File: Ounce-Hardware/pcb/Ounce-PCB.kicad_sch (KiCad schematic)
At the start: 5 parts, among them U1 RaspberryPi_Pico_W, U2 RaspberryPi_Pico, U3 RaspberryPi_Pico, U4 RaspberryPi_Pico, U5 RaspberryPi_Pico

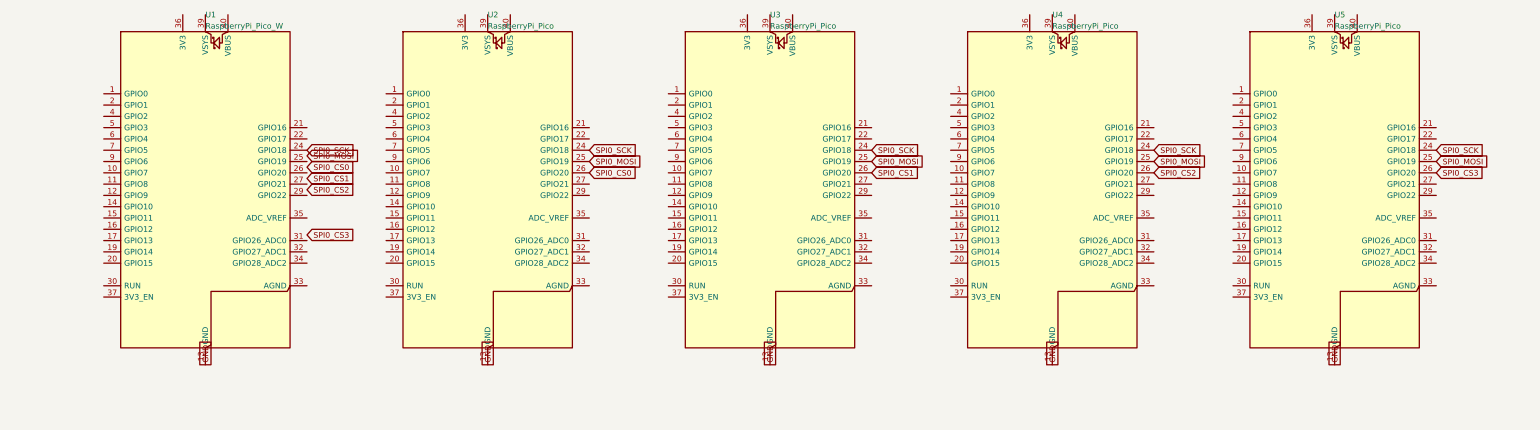
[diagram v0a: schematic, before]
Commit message: Wire the schematic to the four-MISO GPIO standard
The schematic still described the old single-MISO design, and not correctly:

  - servants took MOSI on GPIO19 (pin 25), which under the current standard is
    the servant's MISO *output*. Driving that from the master's MOSI would have
    put two outputs on one wire.
  - servants took CS on GPIO20 (pin 26) rather than GPIO17 (pin 22).
  - the master's MOSI and all four CS labels sat half a pitch (1.27mm) off grid,
    touching no pin at all.
  - no MISO net existed anywhere.

Now carries the eleven nets the firmware actually uses: SCK and MOSI shared,
CS0-3 point to point from GP21/22/26/27 to each servant's GP17, and MISO0-3
back from each servant's GP19 to GP0/4/16/20 on the master.

Two things had to be fixed before any of that could connect:

Labels do not attach to pins by sharing coordinates - ERC reported every label
dangling, including the GND ones that predate this change. Each net now has a
5.08mm wire stub from the pin with the label on its free end.

U1 contributed no pins at all. RaspberryPi_Pico_W was stored as a derived
symbol (extends), which KiCad does not resolve inside a schematic's own symbol
cache, so the master had no connectable pins and reported lib_symbol_mismatch.
Flattened to a standalone symbol carrying its own 40 pins, keeping the Pico W
name and datasheet.

Verified by exporting the netlist with kicad-cli and checking every node
against spi_master.cpp - all eleven nets match pin for pin. ERC now reports no
dangling labels, no isolated labels and no unconnected wire endpoints, down
from 27 such errors.

SVG re-exported to match. The board file is still an outline only: pulling
these nets in needs Update PCB from Schematic in pcbnew, which the CLI cannot
do.

Co-Authored-By: Claude Opus 5 <noreply@anthropic.com>
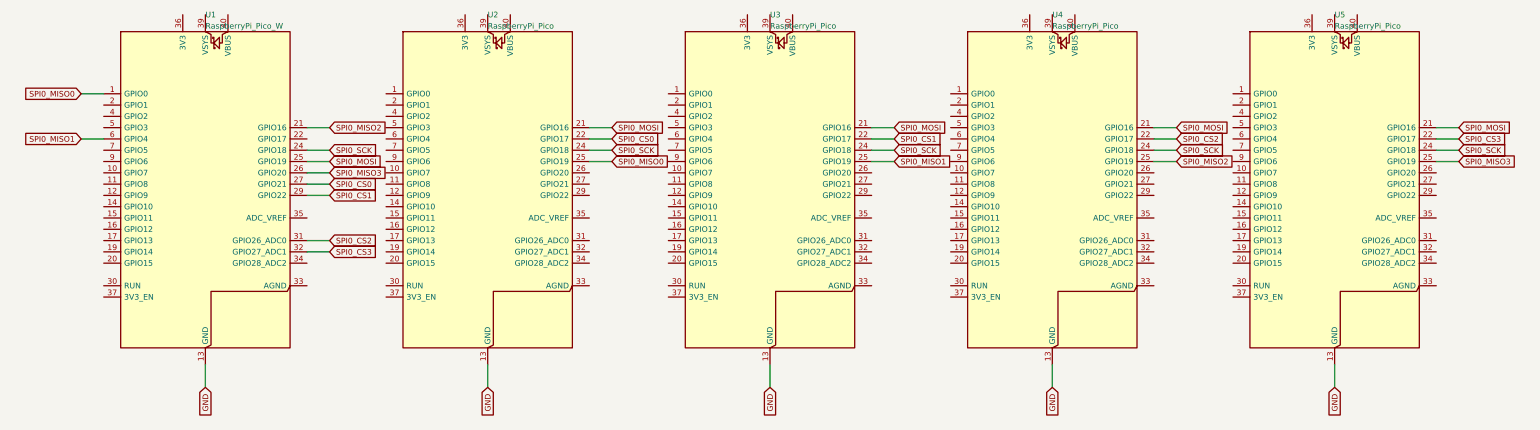
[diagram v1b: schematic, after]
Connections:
- net GND: now also U1.13 (GND), U1.18 (GND), U1.23 (GND), U1.28 (GND), U1.3 (GND), U1.38 (GND), U1.8 (GND)
- net SPI0_CS0: now also U1.27 (GPIO21), U2.22 (GPIO17); no longer U2.26 (GPIO20)
- net SPI0_CS1: now also U1.29 (GPIO22), U3.22 (GPIO17); no longer U3.26 (GPIO20)
- net SPI0_CS2: now also U1.31 (GPIO26_ADC0), U4.22 (GPIO17); no longer U4.26 (GPIO20)
- net SPI0_CS3: now also U1.32 (GPIO27_ADC1), U5.22 (GPIO17); no longer U5.26 (GPIO20)
- net SPI0_MOSI: now also U1.25 (GPIO19), U2.21 (GPIO16), U3.21 (GPIO16), U4.21 (GPIO16), U5.21 (GPIO16); no longer U2.25 (GPIO19), U3.25 (GPIO19), U4.25 (GPIO19), U5.25 (GPIO19)
- net SPI0_SCK: now also U1.24 (GPIO18)
- new net SPI0_MISO0: U1.1 (GPIO0), U2.25 (GPIO19)
- new net SPI0_MISO1: U1.6 (GPIO4), U3.25 (GPIO19)
- new net SPI0_MISO2: U1.21 (GPIO16), U4.25 (GPIO19)
- new net SPI0_MISO3: U1.26 (GPIO20), U5.25 (GPIO19)
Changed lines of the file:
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@@
     )
-  )
-  (global_label "SPI0_SCK" (shape input) (at 73.66 53.34 0)
-    (effects (font (size 1.27 1.27)) (justify left))
-  )
-  (global_label "SPI0_MOSI" (shape input) (at 73.66 54.61 0)
-    (effects (font (size 1.27 1.27)) (justify left))
-  )
-  (global_label "SPI0_CS0" (shape input) (at 73.66 57.15 0)
-    (effects (font (size 1.27 1.27)) (justify left))
-  )
-  (global_label "SPI0_CS1" (shape input) (at 73.66 59.69 0)
-    (effects (font (size 1.27 1.27)) (justify left))
-  )
-  (global_label "SPI0_CS2" (shape input) (at 73.66 62.23 0)
-    (effects (font (size 1.27 1.27)) (justify left))
-  )
-  (global_label "SPI0_CS3" (shape input) (at 73.66 72.39 0)
-    (effects (font (size 1.27 1.27)) (justify left))
-  )
-  (global_label "GND" (shape passive) (at 50.80 101.60 270)
-    (effects (font (size 1.27 1.27)) (justify left))
-  )
-  (global_label "SPI0_SCK" (shape input) (at 137.16 53.34 0)
-    (effects (font (size 1.27 1.27)) (justify left))
-  )
-  (global_label "SPI0_MOSI" (shape input) (at 137.16 55.88 0)
-    (effects (font (size 1.27 1.27)) (justify left))
-  )
-  (global_label "SPI0_CS0" (shape input) (at 137.16 58.42 0)
-    (effects (font (size 1.27 1.27)) (justify left))
-  )
-  (global_label "GND" (shape passive) (at 114.30 101.60 270)
-    (effects (font (size 1.27 1.27)) (justify left))
-  )
-  (global_label "SPI0_SCK" (shape input) (at 200.66 53.34 0)
-    (effects (font (size 1.27 1.27)) (justify left))
-  )
-  (global_label "SPI0_MOSI" (shape input) (at 200.66 55.88 0)
-    (effects (font (size 1.27 1.27)) (justify left))
-  )
-  (global_label "SPI0_CS1" (shape input) (at 200.66 58.42 0)
-    (effects (font (size 1.27 1.27)) (justify left))
-  )
-  (global_label "GND" (shape passive) (at 177.80 101.60 270)
-    (effects (font (size 1.27 1.27)) (justify left))
-  )
-  (global_label "SPI0_SCK" (shape input) (at 264.16 53.34 0)
-    (effects (font (size 1.27 1.27)) (justify left))
-  )
-  (global_label "SPI0_MOSI" (shape input) (at 264.16 55.88 0)
-    (effects (font (size 1.27 1.27)) (justify left))
-  )
-  (global_label "SPI0_CS2" (shape input) (at 264.16 58.42 0)
-    (effects (font (size 1.27 1.27)) (justify left))
-  )
-  (global_label "GND" (shape passive) (at 241.30 101.60 270)
-    (effects (font (size 1.27 1.27)) (justify left))
-  )
-  (global_label "SPI0_SCK" (shape input) (at 327.66 53.34 0)
-    (effects (font (size 1.27 1.27)) (justify left))
-  )
-  (global_label "SPI0_MOSI" (shape input) (at 327.66 55.88 0)
-    (effects (font (size 1.27 1.27)) (justify left))
-  )
-  (global_label "SPI0_CS3" (shape input) (at 327.66 58.42 0)
-    (effects (font (size 1.27 1.27)) (justify left))
-  )
-  (global_label "GND" (shape passive) (at 304.80 101.60 270)
-    (effects (font (size 1.27 1.27)) (justify left))
   )
   (sheet_instances (path "/" (page "1")))
@@
     )
   )
+  (wire (pts (xy 73.66 53.34) (xy 78.74 53.34))
+    (stroke (width 0) (type default))
+  )
+  (wire (pts (xy 73.66 55.88) (xy 78.74 55.88))
+    (stroke (width 0) (type default))
+  )
+  (wire (pts (xy 73.66 60.96) (xy 78.74 60.96))
+    (stroke (width 0) (type default))
+  )
+  (wire (pts (xy 73.66 63.50) (xy 78.74 63.50))
+    (stroke (width 0) (type default))
+  )
+  (wire (pts (xy 73.66 73.66) (xy 78.74 73.66))
+    (stroke (width 0) (type default))
+  )
+  (wire (pts (xy 73.66 76.20) (xy 78.74 76.20))
+    (stroke (width 0) (type default))
+  )
+  (wire (pts (xy 27.94 40.64) (xy 22.86 40.64))
+    (stroke (width 0) (type default))
+  )
+  (wire (pts (xy 27.94 50.80) (xy 22.86 50.80))
+    (stroke (width 0) (type default))
+  )
+  (wire (pts (xy 73.66 48.26) (xy 78.74 48.26))
+    (stroke (width 0) (type default))
+  )
+  (wire (pts (xy 73.66 58.42) (xy 78.74 58.42))
+    (stroke (width 0) (type default))
+  )
+  (wire (pts (xy 50.80 101.60) (xy 50.80 106.68))
+    (stroke (width 0) (type default))
+  )
+  (wire (pts (xy 137.16 53.34) (xy 142.24 53.34))
+    (stroke (width 0) (type default))
+  )
+  (wire (pts (xy 137.16 48.26) (xy 142.24 48.26))
+    (stroke (width 0) (type default))
+  )
+  (wire (pts (xy 137.16 50.80) (xy 142.24 50.80))
+    (stroke (width 0) (type default))
+  )
+  (wire (pts (xy 137.16 55.88) (xy 142.24 55.88))
+    (stroke (width 0) (type default))
+  )
+  (wire (pts (xy 114.30 101.60) (xy 114.30 106.68))
+    (stroke (width 0) (type default))
+  )
+  (wire (pts (xy 200.66 53.34) (xy 205.74 53.34))
+    (stroke (width 0) (type default))
+  )
+  (wire (pts (xy 200.66 48.26) (xy 205.74 48.26))
+    (stroke (width 0) (type default))
+  )
+  (wire (pts (xy 200.66 50.80) (xy 205.74 50.80))
+    (stroke (width 0) (type default))
+  )
+  (wire (pts (xy 200.66 55.88) (xy 205.74 55.88))
+    (stroke (width 0) (type default))
+  )
+  (wire (pts (xy 177.80 101.60) (xy 177.80 106.68))
+    (stroke (width 0) (type default))
+  )
+  (wire (pts (xy 264.16 53.34) (xy 269.24 53.34))
+    (stroke (width 0) (type default))
+  )
+  (wire (pts (xy 264.16 48.26) (xy 269.24 48.26))
+    (stroke (width 0) (type default))
+  )
+  (wire (pts (xy 264.16 50.80) (xy 269.24 50.80))
+    (stroke (width 0) (type default))
+  )
+  (wire (pts (xy 264.16 55.88) (xy 269.24 55.88))
+    (stroke (width 0) (type default))
+  )
+  (wire (pts (xy 241.30 101.60) (xy 241.30 106.68))
+    (stroke (width 0) (type default))
+  )
+  (wire (pts (xy 327.66 53.34) (xy 332.74 53.34))
+    (stroke (width 0) (type default))
+  )
+  (wire (pts (xy 327.66 48.26) (xy 332.74 48.26))
+    (stroke (width 0) (type default))
+  )
+  (wire (pts (xy 327.66 50.80) (xy 332.74 50.80))
+    (stroke (width 0) (type default))
+  )
+  (wire (pts (xy 327.66 55.88) (xy 332.74 55.88))
+    (stroke (width 0) (type default))
+  )
+  (wire (pts (xy 304.80 101.60) (xy 304.80 106.68))
+    (stroke (width 0) (type default))
+  )
+  (global_label "SPI0_SCK" (shape input) (at 78.74 53.34 0)
+    (effects (font (size 1.27 1.27)) (justify left))
+  )
+  (global_label "SPI0_MOSI" (shape input) (at 78.74 55.88 0)
+    (effects (font (size 1.27 1.27)) (justify left))
+  )
+  (global_label "SPI0_CS0" (shape input) (at 78.74 60.96 0)
+    (effects (font (size 1.27 1.27)) (justify left))
+  )
+  (global_label "SPI0_CS1" (shape input) (at 78.74 63.50 0)
+    (effects (font (size 1.27 1.27)) (justify left))
+  )
+  (global_label "SPI0_CS2" (shape input) (at 78.74 73.66 0)
+    (effects (font (size 1.27 1.27)) (justify left))
+  )
+  (global_label "SPI0_CS3" (shape input) (at 78.74 76.20 0)
+    (effects (font (size 1.27 1.27)) (justify left))
+  )
+  (global_label "SPI0_MISO0" (shape input) (at 22.86 40.64 180)
+    (effects (font (size 1.27 1.27)) (justify right))
+  )
+  (global_label "SPI0_MISO1" (shape input) (at 22.86 50.80 180)
+    (effects (font (size 1.27 1.27)) (justify right))
+  )
+  (global_label "SPI0_MISO2" (shape input) (at 78.74 48.26 0)
+    (effects (font (size 1.27 1.27)) (justify left))
+  )
+  (global_label "SPI0_MISO3" (shape input) (at 78.74 58.42 0)
+    (effects (font (size 1.27 1.27)) (justify left))
+  )
+  (global_label "GND" (shape input) (at 50.80 106.68 270)
+    (effects (font (size 1.27 1.27)) (justify right))
+  )
+  (global_label "SPI0_SCK" (shape input) (at 142.24 53.34 0)
+    (effects (font (size 1.27 1.27)) (justify left))
+  )
+  (global_label "SPI0_MOSI" (shape input) (at 142.24 48.26 0)
+    (effects (font (size 1.27 1.27)) (justify left))
+  )
+  (global_label "SPI0_CS0" (shape input) (at 142.24 50.80 0)
+    (effects (font (size 1.27 1.27)) (justify left))
+  )
+  (global_label "SPI0_MISO0" (shape input) (at 142.24 55.88 0)
+    (effects (font (size 1.27 1.27)) (justify left))
+  )
+  (global_label "GND" (shape input) (at 114.30 106.68 270)
+    (effects (font (size 1.27 1.27)) (justify right))
+  )
+  (global_label "SPI0_SCK" (shape input) (at 205.74 53.34 0)
+    (effects (font (size 1.27 1.27)) (justify left))
+  )
+  (global_label "SPI0_MOSI" (shape input) (at 205.74 48.26 0)
+    (effects (font (size 1.27 1.27)) (justify left))
+  )
+  (global_label "SPI0_CS1" (shape input) (at 205.74 50.80 0)
+    (effects (font (size 1.27 1.27)) (justify left))
+  )
+  (global_label "SPI0_MISO1" (shape input) (at 205.74 55.88 0)
+    (effects (font (size 1.27 1.27)) (justify left))
+  )
+  (global_label "GND" (shape input) (at 177.80 106.68 270)
+    (effects (font (size 1.27 1.27)) (justify right))
+  )
+  (global_label "SPI0_SCK" (shape input) (at 269.24 53.34 0)
+    (effects (font (size 1.27 1.27)) (justify left))
+  )
+  (global_label "SPI0_MOSI" (shape input) (at 269.24 48.26 0)
+    (effects (font (size 1.27 1.27)) (justify left))
+  )
+  (global_label "SPI0_CS2" (shape input) (at 269.24 50.80 0)
+    (effects (font (size 1.27 1.27)) (justify left))
+  )
+  (global_label "SPI0_MISO2" (shape input) (at 269.24 55.88 0)
+    (effects (font (size 1.27 1.27)) (justify left))
+  )
+  (global_label "GND" (shape input) (at 241.30 106.68 270)
+    (effects (font (size 1.27 1.27)) (justify right))
+  )
+  (global_label "SPI0_SCK" (shape input) (at 332.74 53.34 0)
+    (effects (font (size 1.27 1.27)) (justify left))
+  )
+  (global_label "SPI0_MOSI" (shape input) (at 332.74 48.26 0)
+    (effects (font (size 1.27 1.27)) (justify left))
+  )
+  (global_label "SPI0_CS3" (shape input) (at 332.74 50.80 0)
+    (effects (font (size 1.27 1.27)) (justify left))
+  )
+  (global_label "SPI0_MISO3" (shape input) (at 332.74 55.88 0)
+    (effects (font (size 1.27 1.27)) (justify left))
+  )
+  (global_label "GND" (shape input) (at 304.80 106.68 270)
+    (effects (font (size 1.27 1.27)) (justify right))
+  )
 )

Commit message: Add a Pico 2 W symbol and resync the cached ones
No upstream library has a Pico 2 / Pico 2 W module symbol, so U1 - the master,
which is a Pico 2 W - was drawn as an RP2040 Pico W. The geometry was right,
since Raspberry Pi kept the pinout and form factor identical, but the BOM named
the wrong part.

Ounce-Symbols.kicad_sym now carries RaspberryPi_Pico2_W: the ki-lime Pico
geometry with all 146 alternate pin functions, correct value, RP2350
description and the Pico 2 W datasheet. Built flattened rather than as an
extends-derived symbol, which is what left the old Pico_W with no resolvable
pins.

The netlist now reads 1x RaspberryPi_Pico2_W and 4x RaspberryPi_Pico, which is
what the hardware actually is.

Also replaced the schematic's cached servant symbol. It still held the stripped
copy - 238 lines, no alternates - against a library that is now pristine, which
is what the remaining lib_symbol_mismatch errors were. Refreshed from v2.1.3 at
1013 lines with 146 alternates.

lib_symbol_mismatch is now 0, down from 5. Netlist re-checked against an
explicit expected table after every step: all ten SPI nets still match
spi_master.cpp pin for pin.

Co-Authored-By: Claude Opus 5 <noreply@anthropic.com>
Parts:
- U1: value RaspberryPi_Pico_W -> RaspberryPi_Pico2_W; symbol MCU_Module_RaspberryPi_Pico:RaspberryPi_Pico_W -> Ounce:RaspberryPi_Pico2_W
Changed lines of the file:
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@@
 (kicad_sch (version 20230121) (generator eeschema) (generator_version "7.0")
   (paper "A4")
-  (symbol (lib_id "MCU_Module_RaspberryPi_Pico:RaspberryPi_Pico_W") (at 50.80 63.50 0) (unit 1)
+  (symbol (lib_id "Ounce:RaspberryPi_Pico2_W") (at 50.80 63.50 0) (unit 1)
     (in_bom yes) (on_board yes)
     (property "Reference" "U1" (at 50.80 22.86 0)
       (effects (font (size 1.27 1.27)) (justify left))
     )
-    (property "Value" "RaspberryPi_Pico_W" (at 50.80 25.40 0)
+    (property "Value" "RaspberryPi_Pico2_W" (at 50.80 25.40 0)
       (effects (font (size 1.27 1.27)) (justify left))
     )
